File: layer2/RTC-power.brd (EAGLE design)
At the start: 17.8 x 49.5 mm, 15 parts, among them U1 DS3234, U2 MCP73831

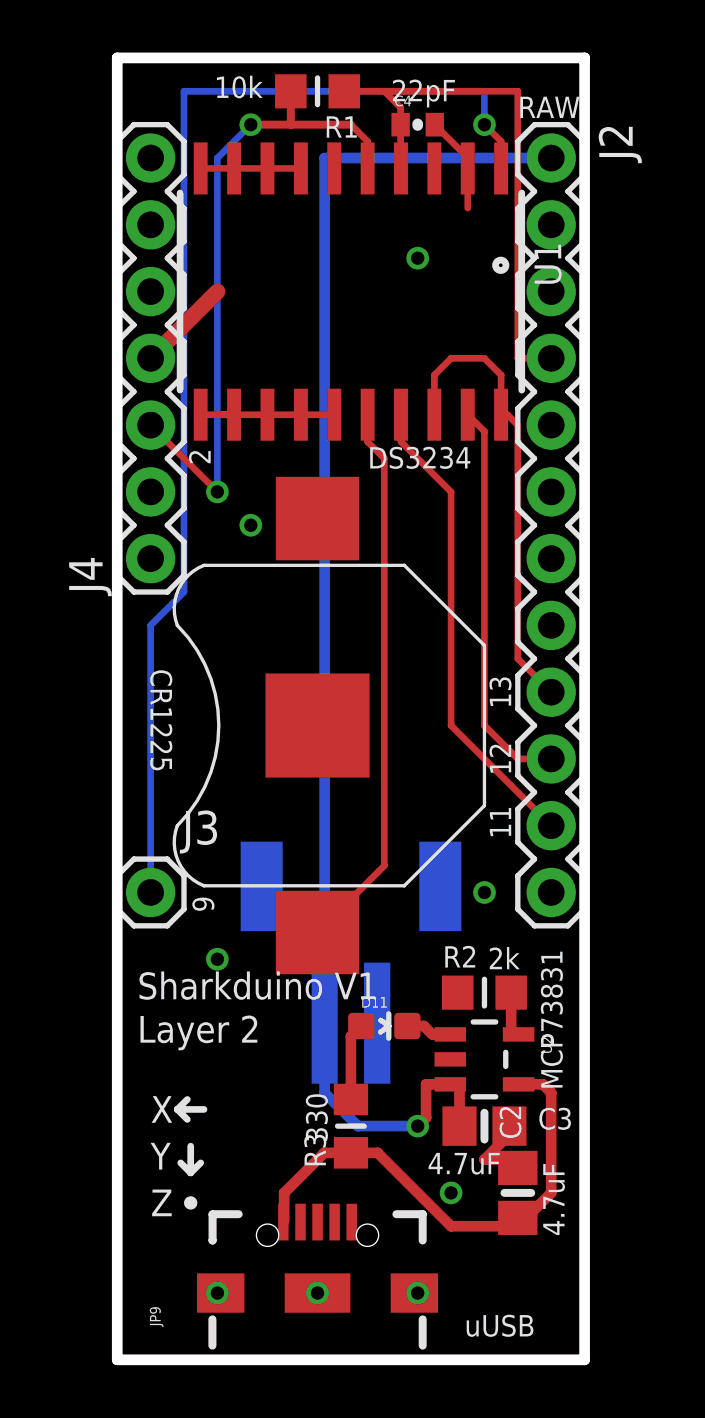
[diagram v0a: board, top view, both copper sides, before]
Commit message: removed via under sd
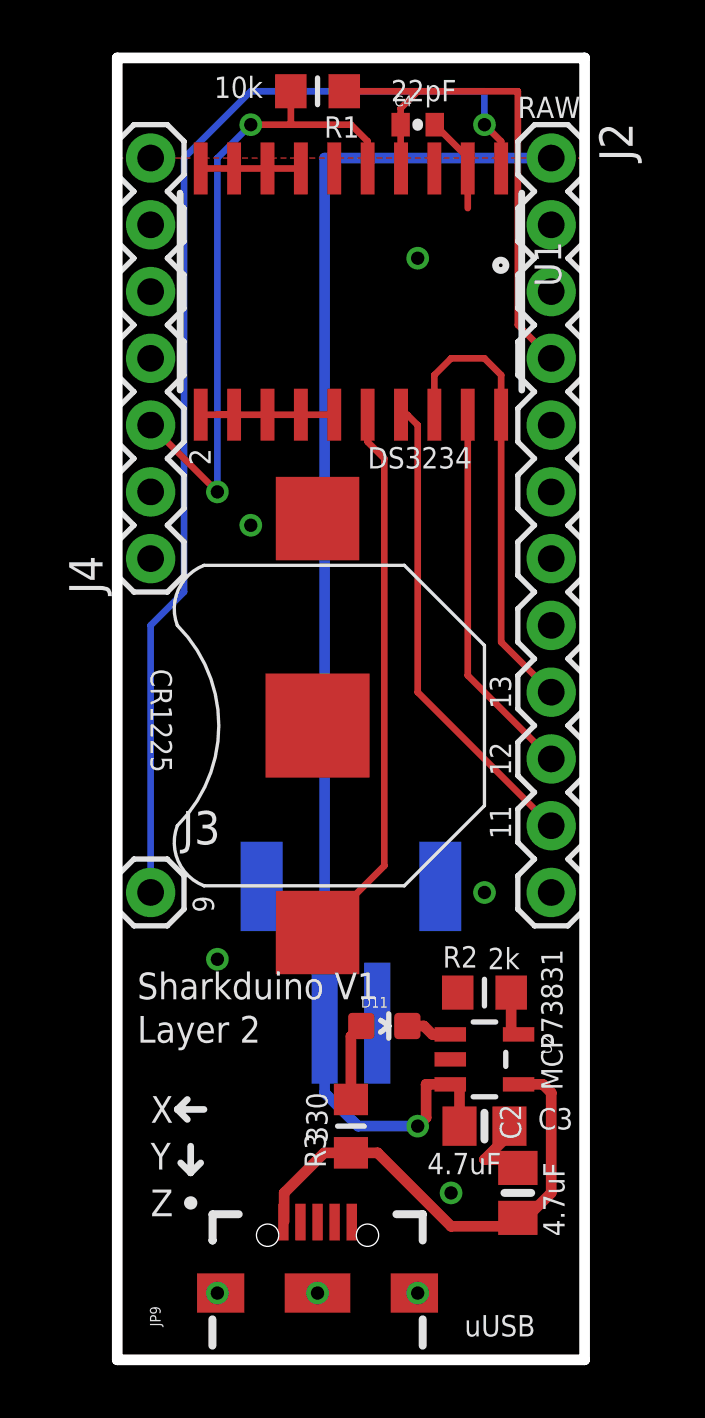
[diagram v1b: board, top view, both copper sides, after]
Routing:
- net GND: track 19.9 -> 16.3 mm
- net RTC_CS: track 45.6 -> 44.1 mm
- net MISO: track 15.2 -> 14.4 mm
- net +3V3: track 21.2 -> 20.5 mm
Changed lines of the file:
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@@
 <setting verticaltext="up"/>
 </settings>
-<grid distance="0.005" unitdist="inch" unit="inch" style="lines" multiple="1" display="yes" altdistance="0.025" altunitdist="inch" altunit="inch"/>
+<grid distance="0.05" unitdist="inch" unit="inch" style="lines" multiple="1" display="yes" altdistance="0.005" altunitdist="inch" altunit="inch"/>
 <layers>
-<layer number="1" name="Top" color="4" fill="1" visible="no" active="yes"/>
-<layer number="16" name="Bottom" color="1" fill="1" visible="no" active="yes"/>
-<layer number="17" name="Pads" color="2" fill="1" visible="no" active="yes"/>
-<layer number="18" name="Vias" color="2" fill="1" visible="no" active="yes"/>
-<layer number="19" name="Unrouted" color="6" fill="1" visible="no" active="yes"/>
-<layer number="20" name="Dimension" color="15" fill="1" visible="no" active="yes"/>
-<layer number="21" name="tPlace" color="16" fill="1" visible="no" active="yes"/>
+<layer number="1" name="Top" color="4" fill="1" visible="yes" active="yes"/>
+<layer number="16" name="Bottom" color="1" fill="1" visible="yes" active="yes"/>
+<layer number="17" name="Pads" color="2" fill="1" visible="yes" active="yes"/>
+<layer number="18" name="Vias" color="2" fill="1" visible="yes" active="yes"/>
+<layer number="19" name="Unrouted" color="6" fill="1" visible="yes" active="yes"/>
+<layer number="20" name="Dimension" color="15" fill="1" visible="yes" active="yes"/>
+<layer number="21" name="tPlace" color="16" fill="1" visible="yes" active="yes"/>
 <layer number="22" name="bPlace" color="14" fill="1" visible="yes" active="yes"/>
-<layer number="23" name="tOrigins" color="15" fill="1" visible="no" active="yes"/>
-<layer number="24" name="bOrigins" color="15" fill="1" visible="no" active="yes"/>
+<layer number="23" name="tOrigins" color="15" fill="1" visible="yes" active="yes"/>
+<layer number="24" name="bOrigins" color="15" fill="1" visible="yes" active="yes"/>
 <layer number="25" name="tNames" color="7" fill="1" visible="no" active="yes"/>
 <layer number="26" name="bNames" color="7" fill="1" visible="no" active="yes"/>
@@
 <via x="13.97" y="46.99" extent="1-16" drill="0.508"/>
 <wire x1="13.97" y1="46.99" x2="13.97" y2="48.26" width="0.254" layer="16"/>
-<wire x1="13.97" y1="48.26" x2="2.54" y2="48.26" width="0.254" layer="16"/>
 <wire x1="14.605" y1="45.325" x2="14.605" y2="46.355" width="0.254" layer="1"/>
 <wire x1="14.605" y1="46.355" x2="13.97" y2="46.99" width="0.254" layer="1"/>
@@
 <wire x1="1.27" y1="17.78" x2="1.27" y2="27.94" width="0.254" layer="16"/>
 <wire x1="1.27" y1="27.94" x2="2.54" y2="29.21" width="0.254" layer="16"/>
-<wire x1="2.54" y1="29.21" x2="2.54" y2="48.26" width="0.254" layer="16"/>
+<wire x1="2.54" y1="29.21" x2="2.54" y2="45.72" width="0.254" layer="16"/>
+<wire x1="2.54" y1="45.72" x2="5.08" y2="48.26" width="0.254" layer="16"/>
+<wire x1="5.08" y1="48.26" x2="13.97" y2="48.26" width="0.254" layer="16"/>
 </signal>
 <signal name="GND">
@@
 <via x="11.43" y="41.91" extent="1-16" drill="0.508"/>
 <polygon width="0.254" layer="1" isolate="0.3048">
-<vertex x="0" y="49.53"/>
-<vertex x="17.78" y="49.53"/>
+<vertex x="0" y="45.72"/>
+<vertex x="17.78" y="45.72"/>
 <vertex x="17.78" y="0"/>
 <vertex x="0" y="0"/>
@@
 <via x="3.81" y="15.24" extent="1-16" drill="0.508"/>
 <via x="13.97" y="17.78" extent="1-16" drill="0.508"/>
-<wire x1="1.27" y1="38.1" x2="3.81" y2="40.64" width="0.6096" layer="1"/>
 <via x="12.7" y="6.35" extent="1-16" drill="0.508"/>
 <contactref element="J4" pad="4"/>
@@
 <contactref element="U1" pad="19"/>
 <contactref element="J2" pad="10"/>
-<wire x1="13.97" y1="24.13" x2="13.97" y2="35.32" width="0.254" layer="1"/>
-<wire x1="13.97" y1="35.32" x2="13.335" y2="35.955" width="0.254" layer="1"/>
-<wire x1="16.51" y1="22.86" x2="15.24" y2="22.86" width="0.254" layer="1"/>
-<wire x1="13.97" y1="24.13" x2="15.24" y2="22.86" width="0.254" layer="1"/>
+<wire x1="13.335" y1="35.955" x2="13.335" y2="26.035" width="0.254" layer="1"/>
+<wire x1="13.335" y1="26.035" x2="16.51" y2="22.86" width="0.254" layer="1"/>
 </signal>
 <signal name="MOSI">
 <contactref element="U1" pad="17"/>
 <contactref element="J2" pad="11"/>
-<wire x1="10.795" y1="35.955" x2="10.795" y2="34.925" width="0.254" layer="1"/>
-<wire x1="10.795" y1="34.925" x2="12.7" y2="33.02" width="0.254" layer="1"/>
-<wire x1="12.7" y1="33.02" x2="12.7" y2="24.13" width="0.254" layer="1"/>
-<wire x1="12.7" y1="24.13" x2="16.51" y2="20.32" width="0.254" layer="1"/>
+<wire x1="11.43" y1="25.4" x2="16.51" y2="20.32" width="0.254" layer="1"/>
+<wire x1="10.795" y1="35.955" x2="11.035" y2="35.955" width="0.254" layer="1"/>
+<wire x1="11.035" y1="35.955" x2="11.43" y2="35.56" width="0.254" layer="1"/>
+<wire x1="11.43" y1="35.56" x2="11.43" y2="25.4" width="0.254" layer="1"/>
 </signal>
 <signal name="INT/SQW">
@@
 <wire x1="9.525" y1="46.355" x2="8.89" y2="46.99" width="0.254" layer="1"/>
 <via x="5.08" y="46.99" extent="1-16" drill="0.508"/>
-<wire x1="8.89" y1="46.99" x2="6.604" y2="46.99" width="0.3048" layer="1"/>
-<wire x1="6.604" y1="46.99" x2="6.604" y2="48.26" width="0.3048" layer="1"/>
-<wire x1="6.604" y1="46.99" x2="5.08" y2="46.99" width="0.3048" layer="1"/>
+<wire x1="8.89" y1="46.99" x2="6.604" y2="46.99" width="0.254" layer="1"/>
+<wire x1="6.604" y1="46.99" x2="6.604" y2="48.26" width="0.254" layer="1"/>
+<wire x1="6.604" y1="46.99" x2="5.08" y2="46.99" width="0.254" layer="1"/>
 <contactref element="J4" pad="3"/>
 <wire x1="3.81" y1="45.72" x2="5.08" y2="46.99" width="0.254" layer="16"/>
@@
 <contactref element="J2" pad="4"/>
 <contactref element="R1" pad="1"/>
-<wire x1="16.51" y1="38.1" x2="15.24" y2="38.1" width="0.254" layer="1"/>
-<wire x1="15.24" y1="38.1" x2="15.24" y2="48.26" width="0.254" layer="1"/>
 <contactref element="C4" pad="1"/>
-<wire x1="8.636" y1="48.26" x2="10.16" y2="48.26" width="0.254" layer="1"/>
-<wire x1="10.16" y1="48.26" x2="15.24" y2="48.26" width="0.254" layer="1"/>
+<wire x1="15.24" y1="39.37" x2="15.24" y2="48.26" width="0.254" layer="1"/>
+<wire x1="8.636" y1="48.26" x2="11.43" y2="48.26" width="0.254" layer="1"/>
+<wire x1="11.43" y1="48.26" x2="15.24" y2="48.26" width="0.254" layer="1"/>
 <wire x1="10.78" y1="46.99" x2="10.78" y2="45.34" width="0.254" layer="1"/>
 <wire x1="10.78" y1="45.34" x2="10.795" y2="45.325" width="0.254" layer="1"/>
-<wire x1="10.78" y1="46.99" x2="10.78" y2="47.64" width="0.254" layer="1"/>
-<wire x1="10.78" y1="47.64" x2="10.16" y2="48.26" width="0.254" layer="1"/>
+<wire x1="16.51" y1="38.1" x2="15.24" y2="39.37" width="0.254" layer="1"/>
+<wire x1="10.78" y1="46.99" x2="10.78" y2="47.61" width="0.254" layer="1"/>
+<wire x1="10.78" y1="47.61" x2="11.43" y2="48.26" width="0.254" layer="1"/>
 </signal>
 <signal name="N$3">
@@
 <wire x1="8.89" y1="7.874" x2="9.906" y2="7.874" width="0.4064" layer="1"/>
 <wire x1="9.906" y1="7.874" x2="12.7" y2="5.08" width="0.4064" layer="1"/>
-<wire x1="12.7" y1="5.08" x2="15.24" y2="5.08" width="0.4064" layer="1"/>
 <wire x1="15.2701" y1="10.48" x2="16.19" y2="10.48" width="0.4064" layer="1"/>
 <wire x1="16.19" y1="10.48" x2="16.51" y2="10.16" width="0.4064" layer="1"/>
 <wire x1="16.51" y1="10.16" x2="16.51" y2="6.35" width="0.4064" layer="1"/>
-<wire x1="16.51" y1="6.35" x2="15.24" y2="5.08" width="0.4064" layer="1"/>
-<wire x1="15.24" y1="5.08" x2="15.24" y2="5.4" width="0" layer="19" extent="1-1"/>
+<wire x1="15.24" y1="5.08" x2="12.7" y2="5.08" width="0.4064" layer="1"/>
+<wire x1="15.24" y1="5.08" x2="16.51" y2="6.35" width="0.4064" layer="1"/>
+<wire x1="15.24" y1="5.4" x2="15.24" y2="5.08" width="0.4064" layer="1"/>
 </signal>
 <signal name="SD_CS">
@@
 <wire x1="14.605" y1="35.955" x2="14.605" y2="37.465" width="0.254" layer="1"/>
 <wire x1="14.605" y1="37.465" x2="13.97" y2="38.1" width="0.254" layer="1"/>
-<wire x1="14.605" y1="35.955" x2="14.845" y2="35.955" width="0.254" layer="1"/>
-<wire x1="14.845" y1="35.955" x2="15.24" y2="35.56" width="0.254" layer="1"/>
-<wire x1="15.24" y1="35.56" x2="15.24" y2="26.67" width="0.254" layer="1"/>
-<wire x1="15.24" y1="26.67" x2="16.51" y2="25.4" width="0.254" layer="1"/>
+<wire x1="14.605" y1="35.955" x2="14.605" y2="27.305" width="0.254" layer="1"/>
+<wire x1="14.605" y1="27.305" x2="16.51" y2="25.4" width="0.254" layer="1"/>
 </signal>
 <signal name="V_RAW">

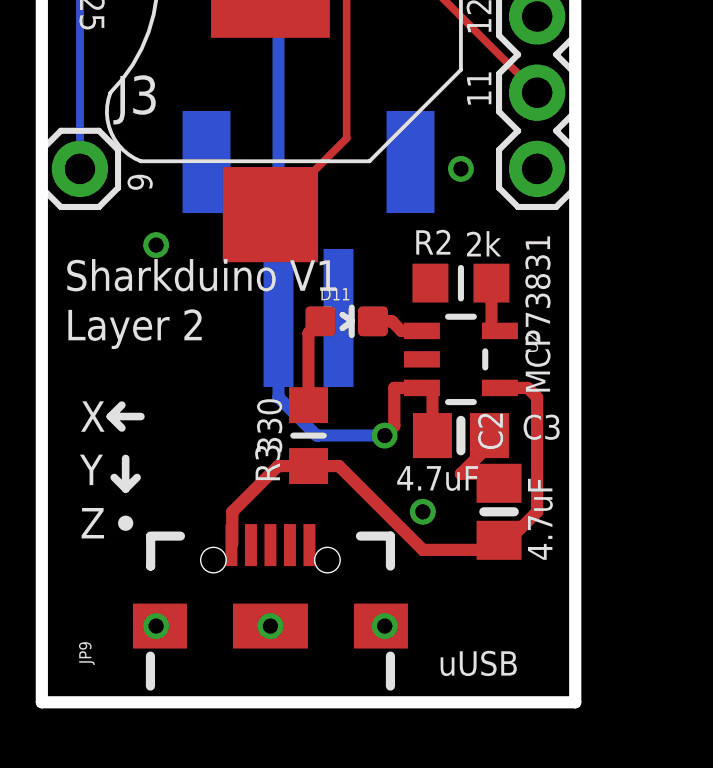
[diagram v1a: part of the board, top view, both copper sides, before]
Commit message: tweaked silk screen and spread out some componets slightly
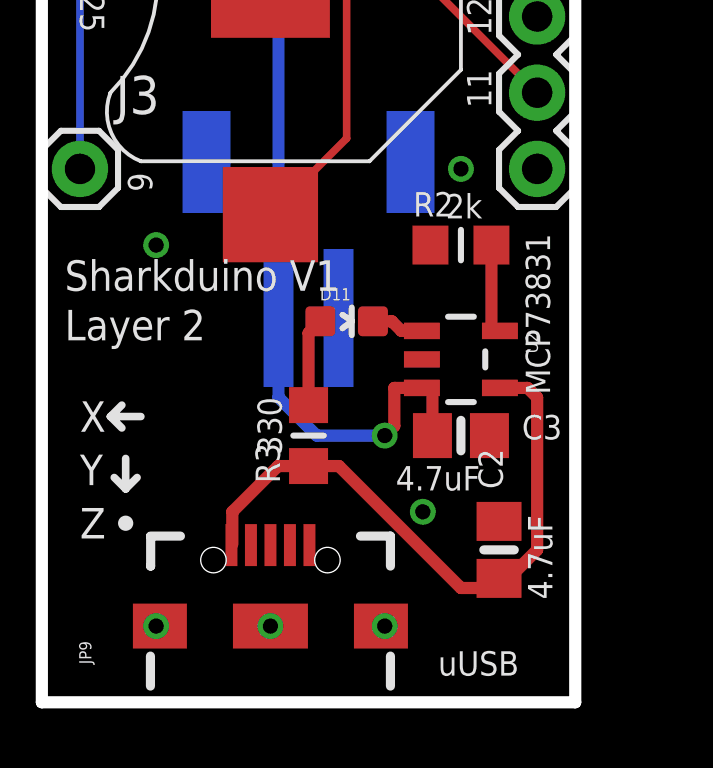
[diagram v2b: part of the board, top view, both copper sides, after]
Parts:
- moved C2 1.27 mm to (15.2, 5.08)
- moved R2 1.27 mm to (14.0, 15.2)
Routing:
- net GND: track 16.3 -> 13.5 mm
- net VIN: track 19.1 -> 20.6 mm
- net PROG: track 1.87 -> 3.14 mm
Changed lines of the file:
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@@
 <text x="1.27" y="26.289" size="0.8128" layer="21" font="vector" ratio="15" rot="SR270">CR1225</text>
 <text x="3.556" y="34.036" size="0.8128" layer="21" font="vector" ratio="15" rot="R90">2</text>
-<text x="17.018" y="4.699" size="0.8128" layer="21" font="vector" ratio="15" rot="R90">4.7uF</text>
+<text x="17.018" y="3.429" size="0.8128" layer="21" font="vector" ratio="15" rot="R90">4.7uF</text>
 <text x="14.605" y="7.874" size="0.8128" layer="21" font="vector" ratio="15" rot="R180">4.7uF</text>
 <text x="8.001" y="8.255" size="0.8128" layer="21" font="vector" ratio="15" rot="R90">330</text>
-<text x="14.097" y="14.859" size="0.8128" layer="21" font="vector" ratio="15">2k</text>
+<text x="13.462" y="16.129" size="0.8128" layer="21" font="vector" ratio="15">2k</text>
 <text x="3.683" y="48.006" size="0.8128" layer="21" font="vector" ratio="15">10k</text>
 <text x="10.414" y="47.879" size="0.8128" layer="21" font="vector" ratio="15">22pF</text>
@@
 <element name="R1" library="microbuilder" package="_0805MP" value="10K" x="7.62" y="48.26" rot="R180"/>
 <element name="R3" library="microbuilder" package="_0805MP" value="330" x="8.89" y="8.89" rot="R90"/>
-<element name="R2" library="microbuilder" package="_0805MP" value="2.0k" x="13.97" y="13.97"/>
-<element name="C2" library="microbuilder" package="0805-NO" value="4.7uF" x="15.24" y="6.35" rot="R90"/>
+<element name="R2" library="microbuilder" package="_0805MP" value="2.0k" x="13.97" y="15.24"/>
+<element name="C2" library="microbuilder" package="0805-NO" value="4.7uF" x="15.24" y="5.08" rot="R90"/>
 <element name="C3" library="microbuilder" package="0805-NO" value="4.7uF" x="13.97" y="8.89"/>
 <element name="C4" library="SparkFun" package="0402-CAP" value="22pF" x="11.43" y="46.99"/>
@@
 <via x="11.43" y="2.54" extent="1-16" drill="0.508"/>
 <wire x1="14.92" y1="8.89" x2="14.92" y2="8.57" width="0.4064" layer="1"/>
-<wire x1="14.92" y1="8.57" x2="13.97" y2="7.62" width="0.4064" layer="1"/>
-<wire x1="13.97" y1="7.62" x2="14.92" y2="7.62" width="0.4064" layer="1"/>
-<wire x1="14.92" y1="7.62" x2="15.24" y2="7.3" width="0.4064" layer="1"/>
 </signal>
 <signal name="MISO">
@@
 <contactref element="R2" pad="2"/>
 <wire x1="15.2701" y1="12.38" x2="14.986" y2="12.38" width="0.254" layer="1"/>
-<wire x1="14.986" y1="12.38" x2="14.986" y2="13.97" width="0.4064" layer="1"/>
+<wire x1="14.986" y1="12.38" x2="14.986" y2="15.24" width="0.4064" layer="1"/>
 </signal>
 <signal name="STAT">
@@
 <wire x1="6.35" y1="5.27" x2="6.32" y2="5.24" width="0.254" layer="1"/>
 <wire x1="8.89" y1="7.874" x2="9.906" y2="7.874" width="0.4064" layer="1"/>
-<wire x1="9.906" y1="7.874" x2="12.7" y2="5.08" width="0.4064" layer="1"/>
 <wire x1="15.2701" y1="10.48" x2="16.19" y2="10.48" width="0.4064" layer="1"/>
 <wire x1="16.19" y1="10.48" x2="16.51" y2="10.16" width="0.4064" layer="1"/>
-<wire x1="16.51" y1="10.16" x2="16.51" y2="6.35" width="0.4064" layer="1"/>
-<wire x1="15.24" y1="5.08" x2="12.7" y2="5.08" width="0.4064" layer="1"/>
-<wire x1="15.24" y1="5.08" x2="16.51" y2="6.35" width="0.4064" layer="1"/>
-<wire x1="15.24" y1="5.4" x2="15.24" y2="5.08" width="0.4064" layer="1"/>
+<wire x1="16.51" y1="10.16" x2="16.51" y2="5.08" width="0.4064" layer="1"/>
+<wire x1="9.906" y1="7.874" x2="13.97" y2="3.81" width="0.4064" layer="1"/>
+<wire x1="13.97" y1="3.81" x2="14.92" y2="3.81" width="0.4064" layer="1"/>
+<wire x1="14.92" y1="3.81" x2="15.24" y2="4.13" width="0.4064" layer="1"/>
+<wire x1="15.24" y1="4.13" x2="15.56" y2="4.13" width="0.4064" layer="1"/>
+<wire x1="15.56" y1="4.13" x2="16.51" y2="5.08" width="0.4064" layer="1"/>
 </signal>
 <signal name="SD_CS">
